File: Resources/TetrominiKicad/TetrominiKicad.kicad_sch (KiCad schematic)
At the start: 19 parts

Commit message: Primordial audio system here! NEEDS WORK
Currently thje circuit is missing deadlines. i want to already upload it so i dont lose progress but i need to find a way to speed up the processing so we don't miss deadlines in the audio task.
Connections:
- net +3.3V: now also DS2.4 (GAIN)
- net ~{AUDIO_SHUTDOWN}: now reaches U1.12 (MOSI/PB15)
- net ~{AUDIO_SHUTDOWN}: now also DS2.5 (~{SD})
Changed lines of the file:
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@@
 	)
 	(no_connect
-		(at 80.01 92.71)
+		(at 102.87 90.17)
 	)
 	(no_connect
-		(at 80.01 102.87)
-	)
-	(no_connect
-		(at 240.03 91.44)
+		(at 80.01 92.71)
 	)
 	(no_connect
-		(at 237.49 91.44)
+		(at 80.01 102.87)
 	)
 	(no_connect
@@
 		(at 80.01 97.79)
 	)
+	(no_connect
+		(at 102.87 87.63)
+	)
 	(wire
 		(pts
@@
 	(wire
 		(pts
+			(xy 102.87 82.55) (xy 115.57 82.55)
+		)
+		(stroke
+			(width 0)
+			(type default)
+		)
+	)
+	(wire
+		(pts
 			(xy 35.56 101.6) (xy 35.56 91.44)
 		)
@@
 	(wire
 		(pts
+			(xy 237.49 91.44) (xy 237.49 99.06)
+		)
+		(stroke
+			(width 0)
+			(type default)
+		)
+	)
+	(wire
+		(pts
 			(xy 68.58 90.17) (xy 80.01 90.17)
 		)
@@
 	(wire
 		(pts
-			(xy 242.57 102.87) (xy 242.57 91.44)
+			(xy 242.57 99.06) (xy 242.57 91.44)
 		)
 		(stroke
@@
 	(wire
 		(pts
+			(xy 240.03 91.44) (xy 240.03 102.87)
+		)
+		(stroke
+			(width 0)
+			(type default)
+		)
+	)
+	(wire
+		(pts
 			(xy 229.87 91.44) (xy 229.87 102.87)
 		)
@@
 	(global_label "AUDIO_VIN"
 		(shape input)
-		(at 245.11 102.87 0)
+		(at 245.11 102.87 270)
 		(fields_autoplaced yes)
 		(effects
@@
 				(size 1.27 1.27)
 			)
-			(justify left)
+			(justify right)
 		)
 		(property "Intersheetrefs" "${INTERSHEET_REFS}"
-			(at 257.7111 102.87 0)
+			(at 245.11 115.4711 90)
 			(hide yes)
 			(show_name no)
@@
 					(size 1.27 1.27)
 				)
-				(justify left)
+				(justify right)
 			)
 		)
@@
 		)
 	)
+	(global_label "~{AUDIO_SHUTDOWN}"
+		(shape input)
+		(at 115.57 82.55 0)
+		(fields_autoplaced yes)
+		(effects
+			(font
+				(size 1.27 1.27)
+			)
+			(justify left)
+		)
+		(property "Intersheetrefs" "${INTERSHEET_REFS}"
+			(at 135.3677 82.55 0)
+			(hide yes)
+			(show_name no)
+			(do_not_autoplace no)
+			(effects
+				(font
+					(size 1.27 1.27)
+				)
+				(justify left)
+			)
+		)
+	)
 	(global_label "AUDIO_BITCLK"
 		(shape input)
@@
 		)
 	)
+	(global_label "~{AUDIO_SHUTDOWN}"
+		(shape input)
+		(at 240.03 102.87 270)
+		(fields_autoplaced yes)
+		(effects
+			(font
+				(size 1.27 1.27)
+			)
+			(justify right)
+		)
+		(property "Intersheetrefs" "${INTERSHEET_REFS}"
+			(at 240.03 122.6677 90)
+			(hide yes)
+			(show_name no)
+			(do_not_autoplace no)
+			(effects
+				(font
+					(size 1.27 1.27)
+				)
+				(justify right)
+			)
+		)
+	)
 	(global_label "BTN_DOWN"
 		(shape input)
@@
 	)
 	(symbol
+		(lib_id "power:+3.3V")
+		(at 237.49 99.06 180)
+		(unit 1)
+		(body_style 1)
+		(exclude_from_sim no)
+		(in_bom yes)
+		(on_board yes)
+		(in_pos_files yes)
+		(dnp no)
+		(property "Reference" "#PWR028"
+			(at 237.49 95.25 0)
+			(hide yes)
+			(show_name no)
+			(do_not_autoplace no)
+			(effects
+				(font
+					(size 1.27 1.27)
+				)
+			)
+		)
+		(property "Value" "+3.3V"
+			(at 237.236 102.108 0)
+			(show_name no)
+			(do_not_autoplace no)
+			(effects
+				(font
+					(size 0.889 0.889)
+				)
+			)
+		)
+		(property "Footprint" ""
+			(at 237.49 99.06 0)
+			(hide yes)
+			(show_name no)
+			(do_not_autoplace no)
+			(effects
+				(font
+					(size 1.27 1.27)
+				)
+			)
+		)
+		(property "Datasheet" ""
+			(at 237.49 99.06 0)
+			(hide yes)
+			(show_name no)
+			(do_not_autoplace no)
+			(effects
+				(font
+					(size 1.27 1.27)
+				)
+			)
+		)
+		(property "Description" "Power symbol creates a global label with name \"+3.3V\""
+			(at 237.49 99.06 0)
+			(hide yes)
+			(show_name no)
+			(do_not_autoplace no)
+			(effects
+				(font
+					(size 1.27 1.27)
+				)
+			)
+		)
+		(pin "1"
+		)
+		(instances
+			(project "TetrominiKicad"
+				(path "/2d640f78-baf6-4866-abfa-b8b1a428b5a4"
+					(reference "#PWR028")
+					(unit 1)
+				)
+			)
+		)
+	)
+	(symbol
 		(lib_id "Device:C_Small")
 		(at 207.01 115.57 0)
@@
 	(symbol
 		(lib_id "power:GND")
-		(at 242.57 102.87 0)
+		(at 242.57 99.06 0)
 		(unit 1)
 		(body_style 1)
@@
 		(dnp no)
 		(property "Reference" "#PWR019"
-			(at 242.57 109.22 0)
+			(at 242.57 105.41 0)
 			(hide yes)
 			(show_name no)
@@
 		)
 		(property "Value" "GND"
-			(at 244.602 106.934 0)
+			(at 244.602 102.616 0)
 			(show_name no)
 			(do_not_autoplace no)
@@
 		)
 		(property "Footprint" ""
-			(at 242.57 102.87 0)
+			(at 242.57 99.06 0)
 			(hide yes)
 			(show_name no)
@@
 		)
 		(property "Datasheet" ""
-			(at 242.57 102.87 0)
+			(at 242.57 99.06 0)
 			(hide yes)
 			(show_name no)
@@
 		)
 		(property "Description" "Power symbol creates a global label with name \"GND\" , ground"
-			(at 242.57 102.87 0)
+			(at 242.57 99.06 0)
 			(hide yes)
 			(show_name no)

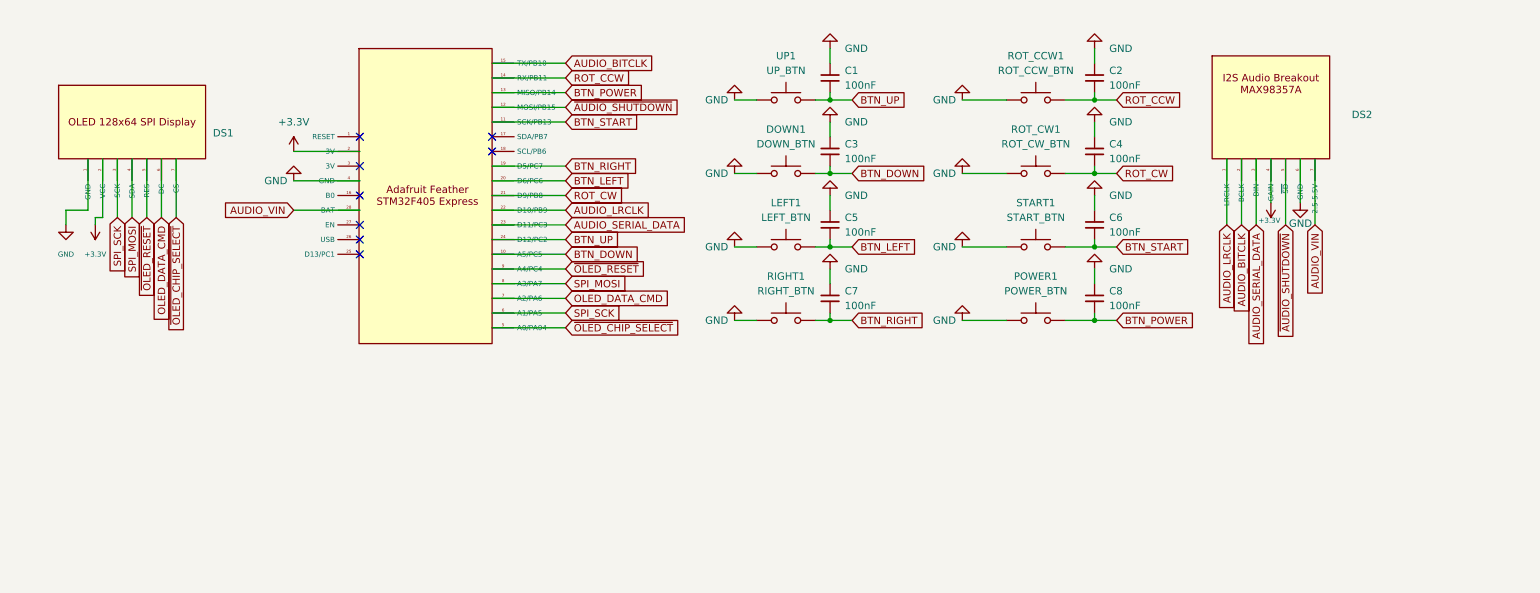
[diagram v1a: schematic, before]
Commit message: MIDILOADER AND GAMEPLAY FINISHED! And updated README and Schematics
Very complete commit!
- Finished Melody loading by improving synthesization and adding envelopes
- Added full playfield logic
- Finalized Rev 1 of PCB and Schematic with RC Hardware Debouncing
- Added all of those things to README
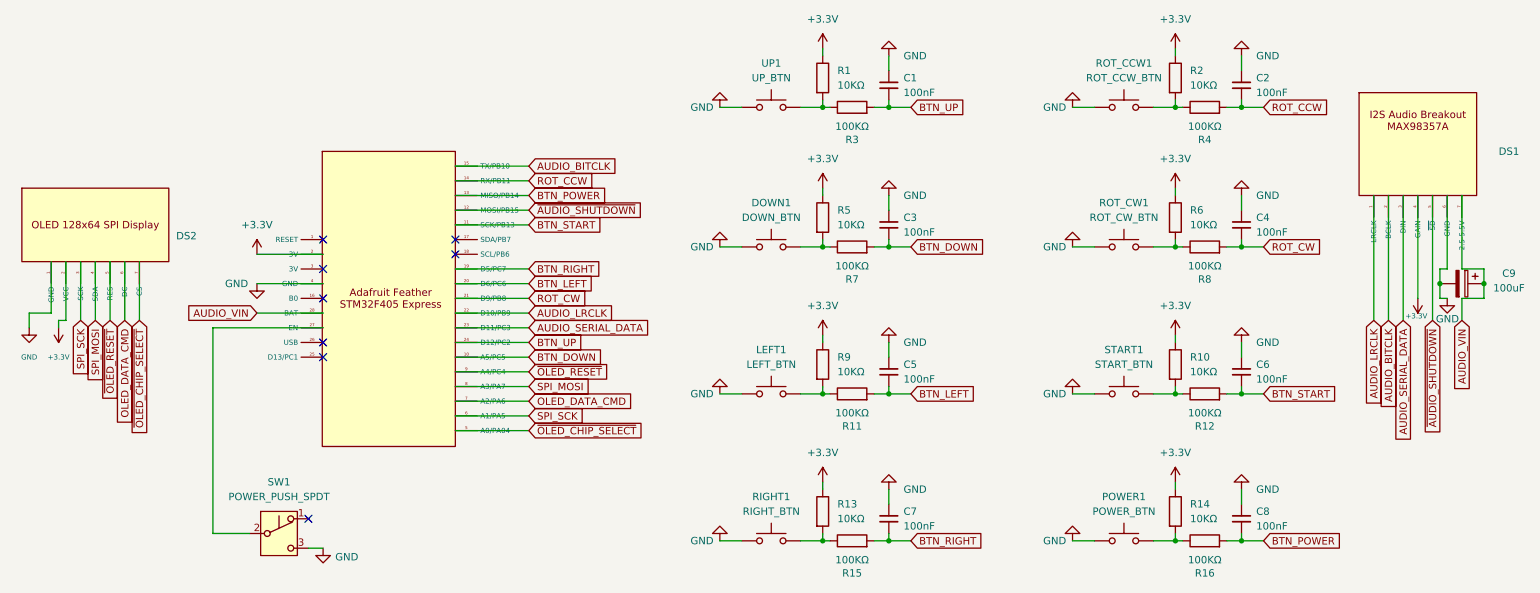
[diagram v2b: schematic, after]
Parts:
- added C9: 100uF, Capacitor_THT:CP_Radial_D5.0mm_P2.00mm, symbol Device:C_Polarized
- added R1, R10, R13, R14, R2, R5, R6, R9: 10KΩ, Resistor_THT:R_Axial_DIN0207_L6.3mm_D2.5mm_P7.62mm_Horizontal, symbol Device:R
- added R11, R12, R15, R16, R3, R4, R7, R8: 100KΩ, Resistor_THT:R_Axial_DIN0207_L6.3mm_D2.5mm_P7.62mm_Horizontal, symbol Device:R
- added SW1: POWER_PUSH_SPDT, Connector_PinHeader_2.54mm:PinHeader_1x03_P2.54mm_Vertical, symbol Switch:SW_Push_SPDT
- C1, C2, C3, C4, C5, C6, C7, C8: footprint (none) -> Capacitor_THT:C_Disc_D5.0mm_W2.5mm_P5.00mm
- DOWN1, LEFT1, POWER1, RIGHT1, ROT_CCW1, ROT_CW1, START1, UP1: footprint (none) -> Button_Switch_THT:SW_PUSH_6mm
- DS1: renamed from DS2; footprint (none) -> Connector_PinSocket_2.54mm:PinSocket_1x07_P2.54mm_Vertical
- DS2: renamed from DS1; footprint Display:OLED-128O064D -> Connector_PinSocket_2.54mm:PinSocket_1x07_P2.54mm_Vertical
- U1: footprint (none) -> Module:Adafruit_Feather
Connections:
- net +3.3V: now also R1.1, R10.1, R13.1, R14.1, R2.1, R5.1, R6.1, R9.1
- net AUDIO_VIN: now also C9.1
- net BTN_DOWN: now also R7.2; no longer DOWN1.2
- net BTN_LEFT: now also R11.2; no longer LEFT1.2
- net BTN_POWER: now also R16.2; no longer POWER1.2
- net BTN_RIGHT: now also R15.2; no longer RIGHT1.2
- net BTN_START: now also R12.2; no longer START1.2
- net BTN_UP: now also R3.2; no longer UP1.2
- net GND: now also C9.2, SW1.3 (C)
- net ROT_CCW: now also R4.2; no longer ROT_CCW1.2
- net ROT_CW: now also R8.2; no longer ROT_CW1.2
- net at U1.27 (EN): now also SW1.2 (B)
- new net: R1.2, R3.1, UP1.2
- new net: R13.2, R15.1, RIGHT1.2
- new net: R2.2, R4.1, ROT_CCW1.2
- new net: LEFT1.2, R11.1, R9.2
- new net: R10.2, R12.1, START1.2
- new net: POWER1.2, R14.2, R16.1
- new net: DOWN1.2, R5.2, R7.1
- new net: R6.2, R8.1, ROT_CW1.2
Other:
- moved on the sheet: C1, DOWN1, DS1, DS2, LEFT1, POWER1, RIGHT1, ROT_CCW1, ROT_CW1, START1, UP1
